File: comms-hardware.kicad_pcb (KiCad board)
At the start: 4 copper layers, 92.5 x 92.5 mm, 313 parts, among them U1 TXCO_TG_5021CG, U10 CC1120, U12 ADT7420, U14 OPA320, U16 RF5110G, U18 FA_128_, U2 TPS79930, U3 FA_128_, U4 CC1120, U5 STM32F407VG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

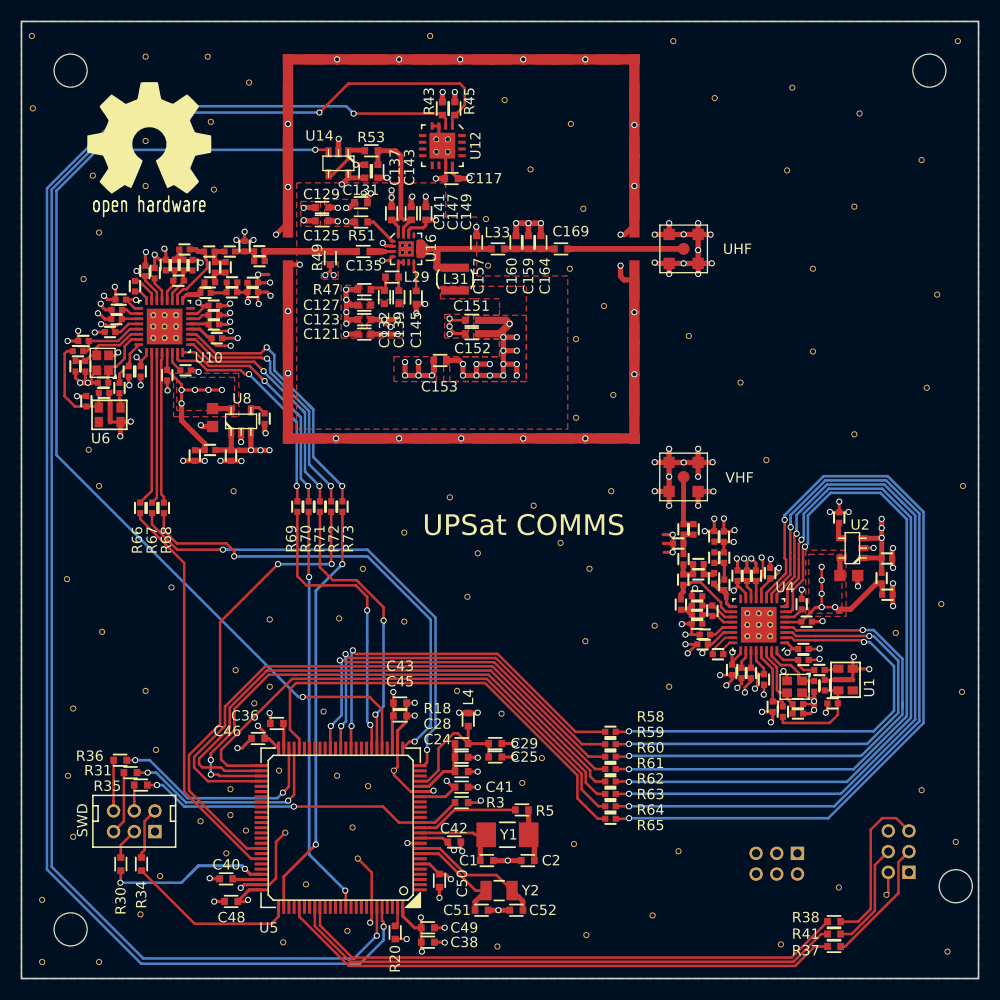
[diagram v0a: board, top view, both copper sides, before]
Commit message: Added MSG Logo on board, modified mounting holes dimensions, modified some copper tracks location
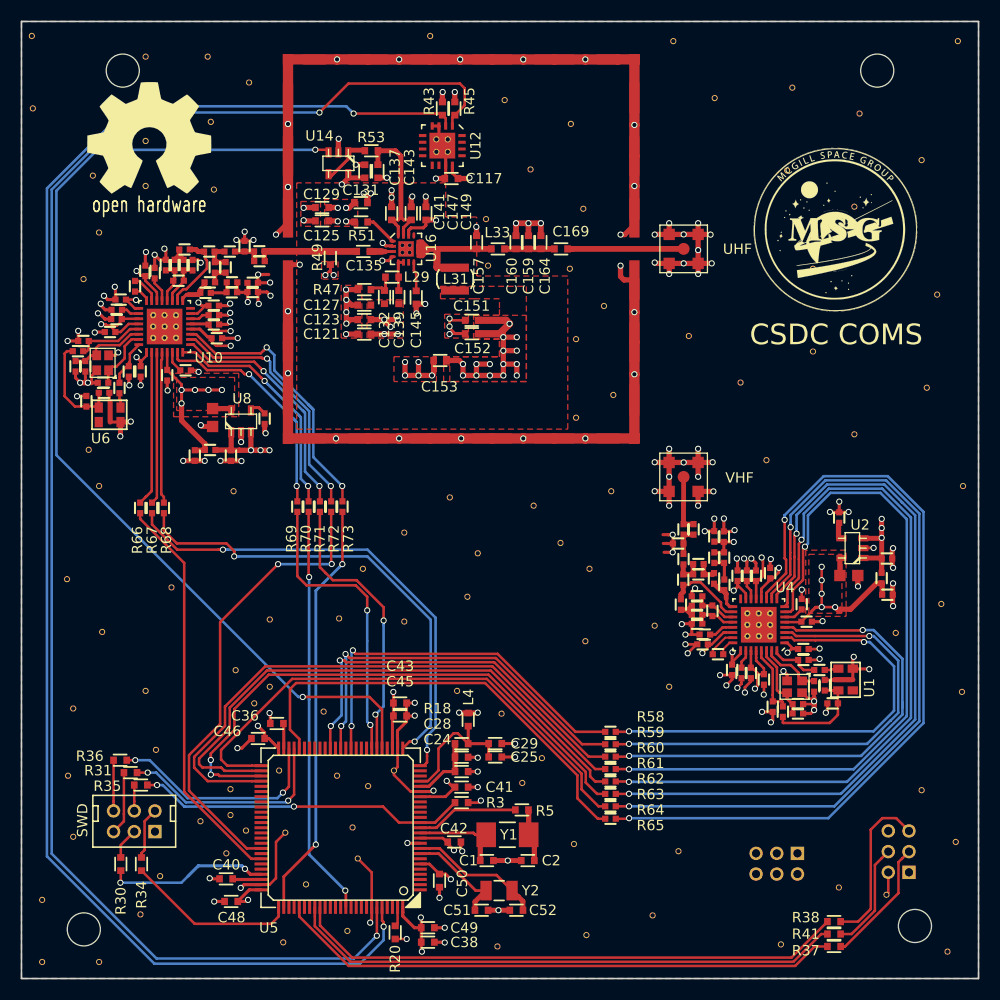
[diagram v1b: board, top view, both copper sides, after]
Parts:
- added G***: LOGO, GraphicV:improved_logo, F.Cu at (181.2, 74.7)
- moved REF** 4.09 mm to (191.4, 142.0)
- moved REF** 1.28 mm to (108.5, 142.3)
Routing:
- net /I2C1_SDA: track 149.4 -> 148.6 mm
- net /I2C1_SCL: track 152.7 -> 152.0 mm
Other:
- board text added: "CSDC COMS"
- board text removed: "In memory of K. Efstathiou"
- board text removed: "UPSat COMMS"
